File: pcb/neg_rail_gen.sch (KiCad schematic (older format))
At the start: 24 parts, among them U5 LM2596S-ADJ

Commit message: populate LCSC BOM for JLCPCB assembly
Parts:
- C29, C32, C34: LCSC (none) -> C19702
- C30: LCSC (none) -> C14663
- FB8: LCSC (none) -> C19330
- R84, R85: LCSC (none) -> C25819
- R86: value 3.07k -> 3k; LCSC (none) -> C4211
- R87: LCSC (none) -> C21190
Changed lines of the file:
@@
 	-1   0    0    1
 $EndComp
-Wire Wire Line
-	5300 3400 5150 3400
 $Comp
 L Device:L L6
@@
 	0    -1   -1   0
 $EndComp
-Wire Wire Line
-	6300 3600 6400 3600
 $Comp
 L Device:CP C31
@@
 F 2 "Capacitor_SMD:C_0603_1608Metric" H 7388 3600 50  0001 C CNN
 F 3 "~" H 7350 3750 50  0001 C CNN
+F 4 "C19702" H 7235 3804 50  0001 C CNN "LCSC"
 	1    7350 3750
 	-1   0    0    1
@@
 	0    -1   -1   0
 $EndComp
-Wire Wire Line
-	8150 3600 8150 3650
-Text HLabel 9000 4000 2    50   Output ~ 0
-Vo(-5V)
-Connection ~ 8150 3600
 $Comp
 L Device:C C34
@@
 F 2 "Capacitor_SMD:C_0603_1608Metric" H 8638 3650 50  0001 C CNN
 F 3 "~" H 8600 3800 50  0001 C CNN
+F 4 "C19702" H 8485 3854 50  0001 C CNN "LCSC"
 	1    8600 3800
 	-1   0    0    1
 $EndComp
-Wire Wire Line
-	8600 3650 8600 3600
-Connection ~ 8600 3600
-Wire Wire Line
-	8600 3600 8150 3600
 $Comp
 L Diode:1N5822 D10
@@
 	0    1    1    0
 $EndComp
-Wire Wire Line
-	6400 3650 6400 3600
-Connection ~ 6400 3600
-Wire Wire Line
-	6400 3600 6500 3600
 $Comp
 L Device:CP C28
@@
 F 2 "Capacitor_SMD:C_0603_1608Metric" H 4188 3400 50  0001 C CNN
 F 3 "~" H 4150 3550 50  0001 C CNN
+F 4 "C19702" H 4265 3696 50  0001 C CNN "LCSC"
 	1    4150 3550
 	1    0    0    -1
 $EndComp
-Text HLabel 2450 3400 0    50   Input ~ 0
-Vi(5V)
-Wire Wire Line
-	3800 3400 4150 3400
-Connection ~ 4150 3400
-Connection ~ 3800 3400
-Wire Wire Line
-	5800 3800 5800 4000
-Wire Wire Line
-	5300 3600 5150 3600
-Wire Wire Line
-	5800 4000 6050 4000
-Wire Wire Line
-	6400 3950 6400 4000
-Connection ~ 6400 4000
-Wire Wire Line
-	6400 4000 6950 4000
-Wire Wire Line
-	6950 3900 6950 4000
-Connection ~ 6950 4000
-Wire Wire Line
-	6950 4000 7350 4000
-Wire Wire Line
-	6800 3600 6950 3600
-Connection ~ 6950 3600
-Connection ~ 7350 4000
-Wire Wire Line
-	7350 3900 7350 4000
-Wire Wire Line
-	8600 4000 8600 3950
-Wire Wire Line
-	8600 4000 8900 4000
-Connection ~ 8600 4000
 $Comp
 L Device:CP C33
@@
 	1    0    0    -1
 $EndComp
-Wire Wire Line
-	8150 3950 8150 4000
-Connection ~ 8150 4000
-Wire Wire Line
-	8150 4000 8600 4000
-Wire Wire Line
-	8100 4000 8150 4000
 $Comp
 L power:GNDPWR #PWR070
@@
 	1    0    0    -1
 $EndComp
-Wire Wire Line
-	8600 3600 9050 3600
-Wire Wire Line
-	7350 3600 7700 3600
-Connection ~ 7350 3600
-Wire Wire Line
-	7350 4000 7700 4000
-Wire Wire Line
-	7700 3650 7700 3600
-Connection ~ 7700 3600
-Wire Wire Line
-	7700 3600 8150 3600
-Wire Wire Line
-	7700 3950 7700 4000
-Connection ~ 7700 4000
-Wire Wire Line
-	7700 4000 7800 4000
 $Comp
 L Device:R R85
@@
 F 2 "Resistor_SMD:R_0603_1608Metric" V 5080 4200 50  0001 C CNN
 F 3 "~" H 5150 4200 50  0001 C CNN
+F 4 "C25819" H 5220 4346 50  0001 C CNN "LCSC"
 	1    5150 4200
 	1    0    0    -1
@@
 F 2 "Resistor_SMD:R_0603_1608Metric" V 4730 3900 50  0001 C CNN
 F 3 "~" H 4800 3900 50  0001 C CNN
+F 4 "C25819" H 4870 4046 50  0001 C CNN "LCSC"
 	1    4800 3900
 	1    0    0    -1
@@
 	1    0    0    -1
 $EndComp
-Wire Wire Line
-	5150 3600 5150 4050
-Wire Wire Line
-	4800 4050 5150 4050
-Connection ~ 5150 4050
-Wire Wire Line
-	5150 4350 5800 4350
-Wire Wire Line
-	5800 4350 5800 4000
-Connection ~ 5800 4000
 $Comp
 L Device:C C30
@@
 F 2 "Capacitor_SMD:C_0603_1608Metric" H 4838 3400 50  0001 C CNN
 F 3 "~" H 4800 3550 50  0001 C CNN
+F 4 "C14663" H 4915 3696 50  0001 C CNN "LCSC"
 	1    4800 3550
 	1    0    0    -1
 $EndComp
-Connection ~ 4800 3400
-Wire Wire Line
-	4800 3700 4800 3750
-Wire Wire Line
-	4150 3400 4800 3400
-Wire Wire Line
-	6950 3600 7350 3600
 $Comp
 L Device:C C35
@@
 P 9250 4400
 F 0 "R86" H 9180 4354 50  0000 R CNN
-F 1 "3.07k" H 9180 4445 50  0000 R CNN
+F 1 "3k" H 9180 4445 50  0000 R CNN
 F 2 "Resistor_SMD:R_0603_1608Metric" V 9180 4400 50  0001 C CNN
 F 3 "~" H 9250 4400 50  0001 C CNN
+F 4 "C4211" H 9180 4454 50  0001 C CNN "LCSC"
 	1    9250 4400
 	-1   0    0    1
 $EndComp
-Wire Wire Line
-	9250 4250 9250 3600
-Wire Wire Line
-	9250 3600 9050 3600
-Connection ~ 9050 3600
-Wire Wire Line
-	6950 4900 6950 4000
-Wire Wire Line
-	9250 4550 9250 4600
-Wire Wire Line
-	6950 4900 9250 4900
 $Comp
 L Device:R R87
@@
 F 2 "Resistor_SMD:R_0603_1608Metric" V 9180 4750 50  0001 C CNN
 F 3 "~" H 9250 4750 50  0001 C CNN
+F 4 "C21190" H 9180 4804 50  0001 C CNN "LCSC"
 	1    9250 4750
 	-1   0    0    1
 $EndComp
-Wire Wire Line
-	9250 4550 9550 4550
-Wire Wire Line
-	9550 4550 9550 3400
-Connection ~ 9250 4550
-Wire Wire Line
-	6300 3400 6400 3400
-Wire Wire Line
-	8950 4250 9250 4250
-Connection ~ 9250 4250
-Wire Wire Line
-	8950 4550 9250 4550
 $Comp
 L power:PWR_FLAG #FLG07
@@
 	1    0    0    -1
 $EndComp
-Connection ~ 8900 4000
-Wire Wire Line
-	8900 4000 8950 4000
-Wire Wire Line
-	2450 3400 2750 3400
 $Comp
 L power:PWR_FLAG #FLG05
@@
 	1    0    0    -1
 $EndComp
-Connection ~ 6050 4000
-Wire Wire Line
-	6050 4000 6400 4000
 $Comp
 L Connector:TestPoint TP30
@@
 	1    0    0    -1
 $EndComp
-Connection ~ 5150 3400
-Wire Wire Line
-	5150 3400 4800 3400
 $Comp
 L Connector:TestPoint TP31
@@
 	1    0    0    -1
 $EndComp
-Connection ~ 6400 3400
-Wire Wire Line
-	6400 3400 9550 3400
 $Comp
 L Connector:TestPoint TP32
@@
 	1    0    0    -1
 $EndComp
-Connection ~ 8950 4000
-Wire Wire Line
-	8950 4000 9000 4000
 $Comp
 L Connector:TestPoint TP34
@@
 F 2 "Inductor_SMD:L_0805_2012Metric_Pad1.05x1.20mm_HandSolder" V 2780 3400 50  0001 C CNN
 F 3 "~" H 2850 3400 50  0001 C CNN
+F 4 "C19330" H 2613 3500 50  0001 C CNN "LCSC"
 	1    2850 3400
 	0    1    1    0
 $EndComp
-Wire Wire Line
-	2950 3400 3200 3400
-Wire Wire Line
-	3800 4350 5150 4350
-Connection ~ 5150 4350
 $Comp
 L Diode:1N5822 D11
@@
 	0    1    1    0
 $EndComp
+Text HLabel 9000 4000 2    50   Output ~ 0
+Vo(-5V)
+Text HLabel 2450 3400 0    50   Input ~ 0
+Vi(5V)
 Text Label 7050 4000 0    50   ~ 0
 -5VO
@@
 -5VO_filtered
 Wire Wire Line
+	5300 3400 5150 3400
+Wire Wire Line
+	6300 3600 6400 3600
+Wire Wire Line
+	8150 3600 8150 3650
+Wire Wire Line
+	8600 3650 8600 3600
+Wire Wire Line
+	8600 3600 8150 3600
+Wire Wire Line
+	6400 3650 6400 3600
+Wire Wire Line
+	6400 3600 6500 3600
+Wire Wire Line
+	3800 3400 4150 3400
+Wire Wire Line
+	5800 3800 5800 4000
+Wire Wire Line
+	5300 3600 5150 3600
+Wire Wire Line
+	5800 4000 6050 4000
+Wire Wire Line
+	6400 3950 6400 4000
+Wire Wire Line
+	6400 4000 6950 4000
+Wire Wire Line
+	6950 3900 6950 4000
+Wire Wire Line
+	6950 4000 7350 4000
+Wire Wire Line
+	6800 3600 6950 3600
+Wire Wire Line
+	7350 3900 7350 4000
+Wire Wire Line
+	8600 4000 8600 3950
+Wire Wire Line
+	8600 4000 8900 4000
+Wire Wire Line
+	8150 3950 8150 4000
+Wire Wire Line
+	8150 4000 8600 4000
+Wire Wire Line
+	8100 4000 8150 4000
+Wire Wire Line
+	8600 3600 9050 3600
+Wire Wire Line
+	7350 3600 7700 3600
+Wire Wire Line
+	7350 4000 7700 4000
+Wire Wire Line
+	7700 3650 7700 3600
+Wire Wire Line
+	7700 3600 8150 3600
+Wire Wire Line
+	7700 3950 7700 4000
+Wire Wire Line
+	7700 4000 7800 4000
+Wire Wire Line
+	5150 3600 5150 4050
+Wire Wire Line
+	4800 4050 5150 4050
+Wire Wire Line
+	5150 4350 5800 4350
+Wire Wire Line
+	5800 4350 5800 4000
+Wire Wire Line
+	4800 3700 4800 3750
+Wire Wire Line
+	4150 3400 4800 3400
+Wire Wire Line
+	6950 3600 7350 3600
+Wire Wire Line
+	9250 4250 9250 3600
+Wire Wire Line
+	9250 3600 9050 3600
+Wire Wire Line
+	6950 4900 6950 4000
+Wire Wire Line
+	9250 4550 9250 4600
+Wire Wire Line
+	6950 4900 9250 4900
+Wire Wire Line
+	9250 4550 9550 4550
+Wire Wire Line
+	9550 4550 9550 3400
+Wire Wire Line
+	6300 3400 6400 3400
+Wire Wire Line
+	8950 4250 9250 4250
+Wire Wire Line
+	8950 4550 9250 4550
+Wire Wire Line
+	8900 4000 8950 4000
+Wire Wire Line
+	2450 3400 2750 3400
+Wire Wire Line
+	6050 4000 6400 4000
+Wire Wire Line
+	5150 3400 4800 3400
+Wire Wire Line
+	6400 3400 9550 3400
+Wire Wire Line
+	8950 4000 9000 4000
+Wire Wire Line
+	2950 3400 3200 3400
+Wire Wire Line
+	3800 4350 5150 4350
+Wire Wire Line
 	3500 3400 3800 3400
 Wire Wire Line
 	3800 3700 3800 4350
+Connection ~ 8150 3600
+Connection ~ 8600 3600
+Connection ~ 6400 3600
+Connection ~ 4150 3400
+Connection ~ 3800 3400
+Connection ~ 6400 4000
+Connection ~ 6950 4000
+Connection ~ 6950 3600
+Connection ~ 7350 4000
+Connection ~ 8600 4000
+Connection ~ 8150 4000
+Connection ~ 7350 3600
+Connection ~ 7700 3600
+Connection ~ 7700 4000
+Connection ~ 5150 4050
+Connection ~ 5800 4000
+Connection ~ 4800 3400
+Connection ~ 9050 3600
+Connection ~ 9250 4550
+Connection ~ 9250 4250
+Connection ~ 8900 4000
+Connection ~ 6050 4000
+Connection ~ 5150 3400
+Connection ~ 6400 3400
+Connection ~ 8950 4000
+Connection ~ 5150 4350
 $EndSCHEMATC

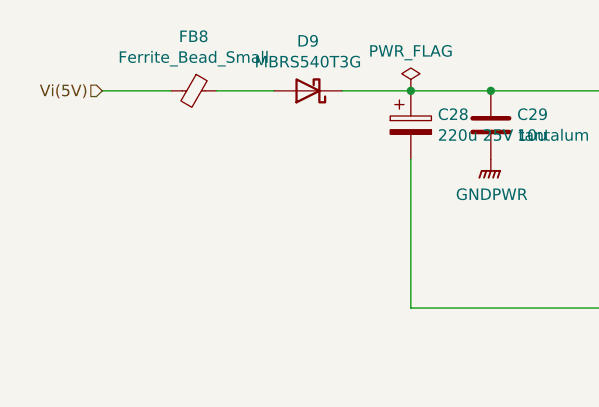
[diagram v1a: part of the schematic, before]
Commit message: add second parallel ferrite bead for input of negative 5V generator
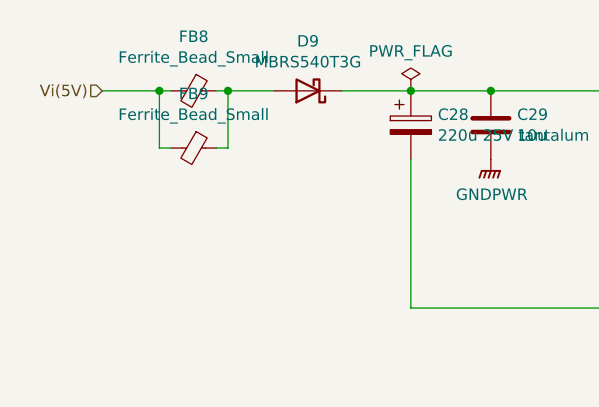
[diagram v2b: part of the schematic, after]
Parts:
- added FB9: Ferrite_Bead_Small, Inductor_SMD:L_0805_2012Metric_Pad1.05x1.20mm_HandSolder, symbol Device:Ferrite_Bead_Small
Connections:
- net Vi(5V): now also FB9.2
- net at D9.2 (A), FB8.1: now also FB9.1
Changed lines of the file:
@@
 	8900 4000 8950 4000
 Wire Wire Line
-	2450 3400 2750 3400
+	2450 3400 2700 3400
 Wire Wire Line
 	6050 4000 6400 4000
@@
 	8950 4000 9000 4000
 Wire Wire Line
-	2950 3400 3200 3400
+	2950 3400 3000 3400
 Wire Wire Line
 	3800 4350 5150 4350
@@
 Connection ~ 8950 4000
 Connection ~ 5150 4350
+$Comp
+L Device:Ferrite_Bead_Small FB9
+U 1 1 5FD504FA
+P 2850 3650
+F 0 "FB9" V 2613 3650 50  0000 C CNN
+F 1 "Ferrite_Bead_Small" V 2704 3650 50  0000 C CNN
+F 2 "Inductor_SMD:L_0805_2012Metric_Pad1.05x1.20mm_HandSolder" V 2780 3650 50  0001 C CNN
+F 3 "~" H 2850 3650 50  0001 C CNN
+F 4 "C19330" H 2613 3750 50  0001 C CNN "LCSC"
+	1    2850 3650
+	0    1    1    0
+$EndComp
+Wire Wire Line
+	2750 3650 2700 3650
+Wire Wire Line
+	2700 3650 2700 3400
+Connection ~ 2700 3400
+Wire Wire Line
+	2700 3400 2750 3400
+Wire Wire Line
+	2950 3650 3000 3650
+Wire Wire Line
+	3000 3650 3000 3400
+Connection ~ 3000 3400
+Wire Wire Line
+	3000 3400 3200 3400
 $EndSCHEMATC

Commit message: fill out more components in BOM with LCSC parts
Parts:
- C28, C31, C33: footprint Capacitor_Tantalum_SMD:CP_EIA-7343-20_Kemet-V_Pad2.25x2.55mm_HandSolder -> Capacitor_Tantalum_SMD:CP_EIA-7343-43_Kemet-X_Pad2.25x2.55mm_HandSolder; LCSC (none) -> C7231
- D10, D11, D9: LCSC (none) -> C14651
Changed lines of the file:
@@
 F 2 "Diode_SMD:D_SMB_Handsoldering" H 3350 3225 50  0001 C CNN
 F 3 "https://www.onsemi.com/pub/Collateral/MBRS540T3-D.PDF" H 3350 3400 50  0001 C CNN
+F 4 "C14651" H 3350 3400 50  0001 C CNN "LCSC"
 	1    3350 3400
 	-1   0    0    1
@@
 F 0 "C31" H 7068 3796 50  0000 L CNN
 F 1 "220u tantalum 25V" H 7068 3705 50  0000 L CNN
-F 2 "Capacitor_Tantalum_SMD:CP_EIA-7343-20_Kemet-V_Pad2.25x2.55mm_HandSolder" H 6988 3600 50  0001 C CNN
+F 2 "Capacitor_Tantalum_SMD:CP_EIA-7343-43_Kemet-X_Pad2.25x2.55mm_HandSolder" H 6988 3600 50  0001 C CNN
 F 3 "~" H 6950 3750 50  0001 C CNN
+F 4 "C7231" H 6950 3750 50  0001 C CNN "LCSC"
 	1    6950 3750
 	1    0    0    -1
@@
 F 2 "Diode_SMD:D_SMB_Handsoldering" H 6400 3625 50  0001 C CNN
 F 3 "https://www.onsemi.com/pub/Collateral/MBRS540T3-D.PDF" H 6400 3800 50  0001 C CNN
+F 4 "C14651" V 6400 3800 50  0001 C CNN "LCSC"
 	1    6400 3800
 	0    1    1    0
@@
 F 0 "C28" H 3918 3596 50  0000 L CNN
 F 1 "220u 25V tantalum" H 3918 3505 50  0000 L CNN
-F 2 "Capacitor_Tantalum_SMD:CP_EIA-7343-20_Kemet-V_Pad2.25x2.55mm_HandSolder" H 3838 3400 50  0001 C CNN
+F 2 "Capacitor_Tantalum_SMD:CP_EIA-7343-43_Kemet-X_Pad2.25x2.55mm_HandSolder" H 3838 3400 50  0001 C CNN
 F 3 "~" H 3800 3550 50  0001 C CNN
+F 4 "C7231" H 3800 3550 50  0001 C CNN "LCSC"
 	1    3800 3550
 	1    0    0    -1
@@
 F 4 "C19702" H 4265 3696 50  0001 C CNN "LCSC"
 	1    4150 3550
-	1    0    0    -1
-$EndComp
-$Comp
-L Device:CP C33
-U 1 1 5FDC37D7
-P 8150 3800
-F 0 "C33" H 8268 3846 50  0000 L CNN
-F 1 "220u tantalum 25V" H 8268 3755 50  0000 L CNN
-F 2 "Capacitor_Tantalum_SMD:CP_EIA-7343-20_Kemet-V_Pad2.25x2.55mm_HandSolder" H 8188 3650 50  0001 C CNN
-F 3 "~" H 8150 3800 50  0001 C CNN
-	1    8150 3800
 	1    0    0    -1
 $EndComp
@@
 F 2 "Diode_SMD:D_SMB_Handsoldering" H 7700 3625 50  0001 C CNN
 F 3 "https://www.onsemi.com/pub/Collateral/MBRS540T3-D.PDF" H 7700 3800 50  0001 C CNN
+F 4 "C14651" V 7700 3800 50  0001 C CNN "LCSC"
 	1    7700 3800
 	0    1    1    0
@@
 Wire Wire Line
 	3000 3400 3200 3400
+$Comp
+L Device:CP C33
+U 1 1 5FDC37D7
+P 8150 3800
+F 0 "C33" H 8268 3846 50  0000 L CNN
+F 1 "220u tantalum 25V" H 8268 3755 50  0000 L CNN
+F 2 "Capacitor_Tantalum_SMD:CP_EIA-7343-43_Kemet-X_Pad2.25x2.55mm_HandSolder" H 8188 3650 50  0001 C CNN
+F 3 "~" H 8150 3800 50  0001 C CNN
+F 4 "C7231" H 8150 3800 50  0001 C CNN "LCSC"
+	1    8150 3800
+	1    0    0    -1
+$EndComp
 $EndSCHEMATC
